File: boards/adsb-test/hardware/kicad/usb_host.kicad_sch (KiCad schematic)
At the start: 13 parts, among them J1101 USB-A (SDR hub), U1101 TPS259621DDA, U1102 USBLC6-2SC6

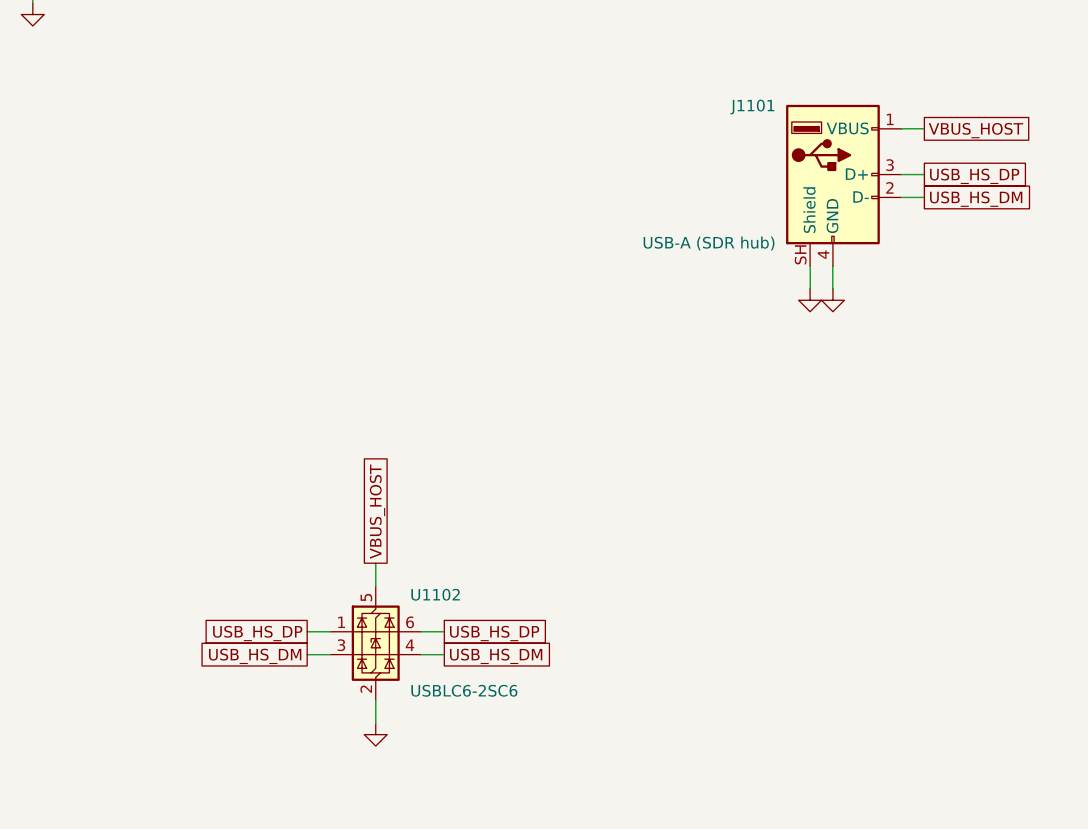
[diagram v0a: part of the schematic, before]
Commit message: ADSB_Test: net classes + diff-pair rules, USB pairs renamed _D_P/_D_N, U201 VSYS drawn at the bottom
Co-Authored-By: Claude Opus 5.5 <noreply@anthropic.com>
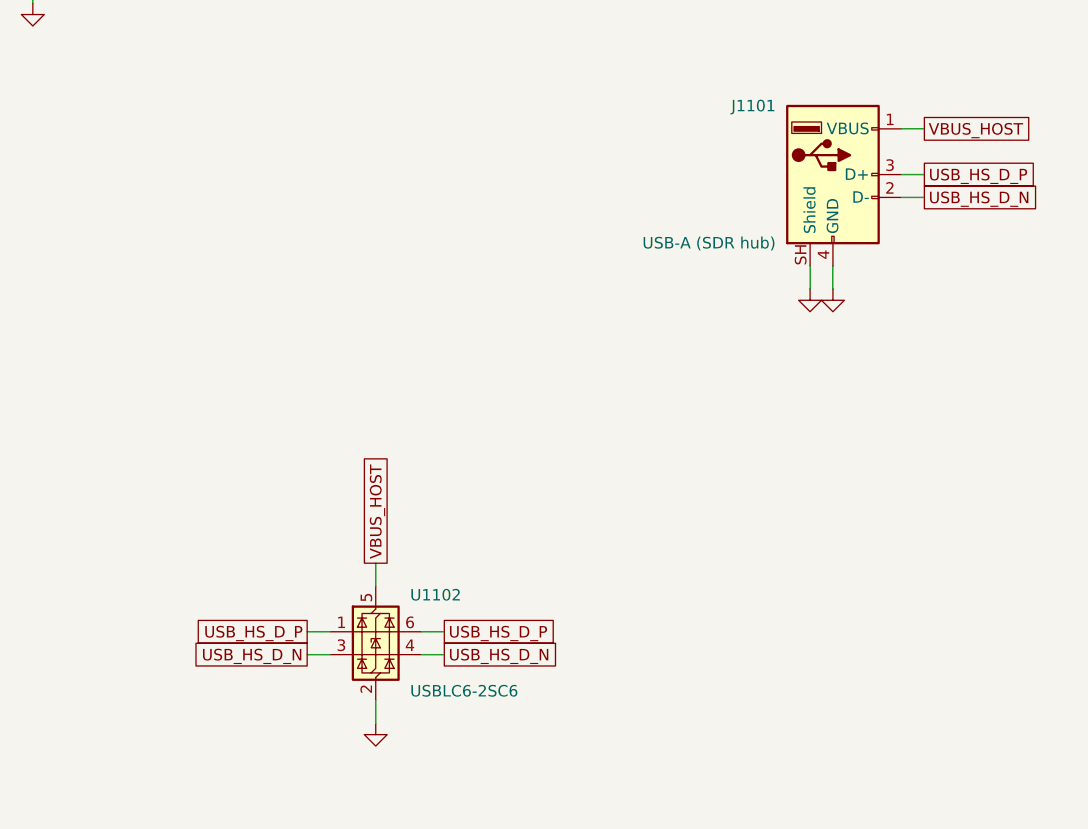
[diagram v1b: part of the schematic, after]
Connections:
- net USB_HS_DM renamed USB_HS_D_N
- net USB_HS_DP renamed USB_HS_D_P

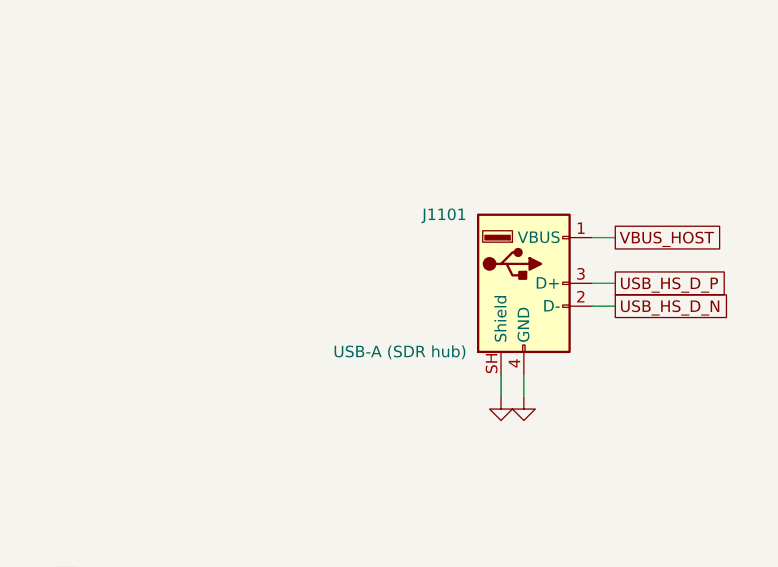
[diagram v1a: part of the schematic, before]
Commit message: ADSB_Test: User USB-C on its own sheet, RP2040 GPIO header + optional I2C, shunt/PWR_FLAG text fixed
Co-Authored-By: Claude Opus 5.5 <noreply@anthropic.com>
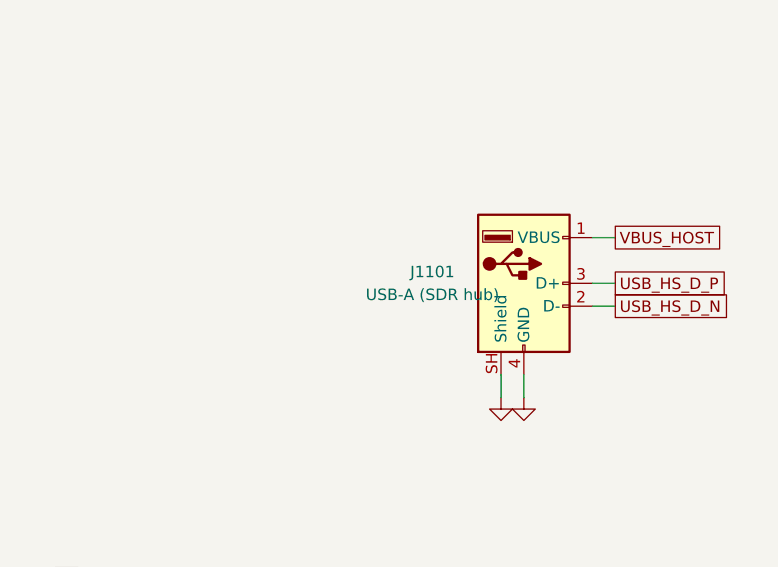
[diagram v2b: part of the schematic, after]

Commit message: ADSB_Test BOM: UK supplier links and upload file, USB-A swapped to Wurth
- make_bom.py: Mouser UK / Farnell UK / RS UK search links per line,
  uk_bom_upload.csv for their BOM tools, uk_stock column.
- J1101 USB-A: Wurth 614004134726 (Molex 0676432910 out of stock).
- Q29 answered (bottom-contact FPC sockets), Q30 updated.

Co-Authored-By: Claude Opus 5.5 <noreply@anthropic.com>
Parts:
- J1101: footprint Connector_USB:USB_A_Molex_67643_Horizontal -> Connector_USB:USB_A_Wuerth_614004134726_Horizontal
